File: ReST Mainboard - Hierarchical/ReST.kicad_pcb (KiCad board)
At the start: 2 copper layers, 100 x 100 mm, 190 parts, among them IC1 AT24C256, P1 CONN_01X02, P10 CONN_02X04, P11 CONN_01X04, P12 CONN_01X04, P13 CONN_01X04, P14 CONN_01X04, P15 USB_OTG, P16 CONN_02X05, P17 CONN_02X05, P18 CONN_02X05, P19 CONN_01X04, P2 CONN_01X03, P20 CONN_01X02, P21 CONN_01X04, P22 CONN_02X03, P23 CONN_02X03, P24 CONN_01X04, P25 CONN_02X03, P26 CONN_02X03, P27 CONN_02X06, P28 CONN_02X02, P29 CONN_01X02, P3 CONN_01X02, P30 CONN_01X02, P31 CONN_01X02, P32 CONN_02X02, P33 CONN_02X02, P34 CONN_02X02, P35 CONN_02X03, P36 CONN_02X03, P37 CONN_02X03, P38 CONN_02X03, P39 CONN_02X03, P4 CONN_01X03, P40 CONN_02X04, P5 CONN_01X03, P6 CONN_01X03, P7 CONN_01X03, P8 CONN_01X03, P9 CONN_01X03, Q1 TBD, Q10 Q_AOT240L, Q11 Q_AOT240L, Q12 Q_AOT240L, Q2 TBD, Q3 TBD, Q4 TBD, Q7 Q_BSH105/IRLML2502, Q8 Q_BSH105/IRLML2502, Q9 Q_BSH105/IRLML2502, U10 USBLC6-2, U2 POLOLU_A4988, U3 ACT4088, U4 SC4626, U5 POLOLU_A4988, U6 POLOLU_A4988, U7 POLOLU_A4988, U8 POLOLU_A4988, U9 STM32F10x/STM32F4x, X1 Crystal_Small

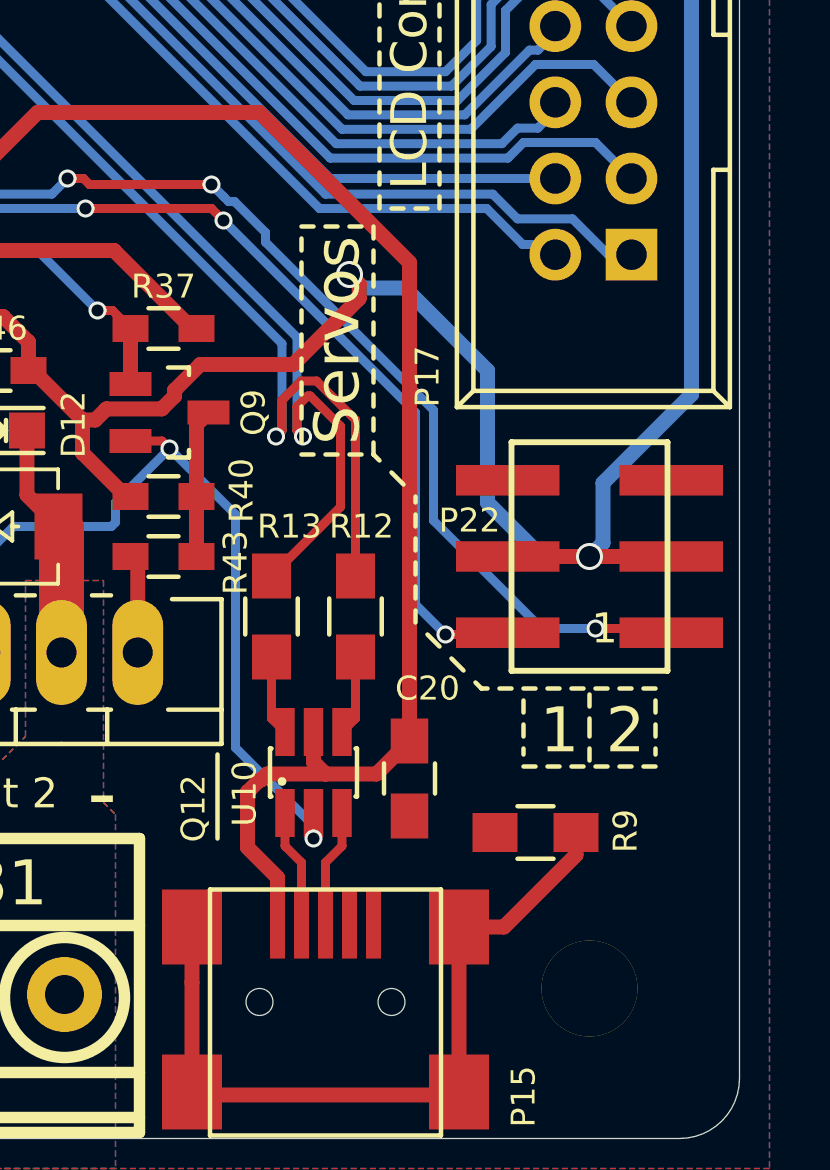
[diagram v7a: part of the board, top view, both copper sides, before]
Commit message: added missing usb pullup
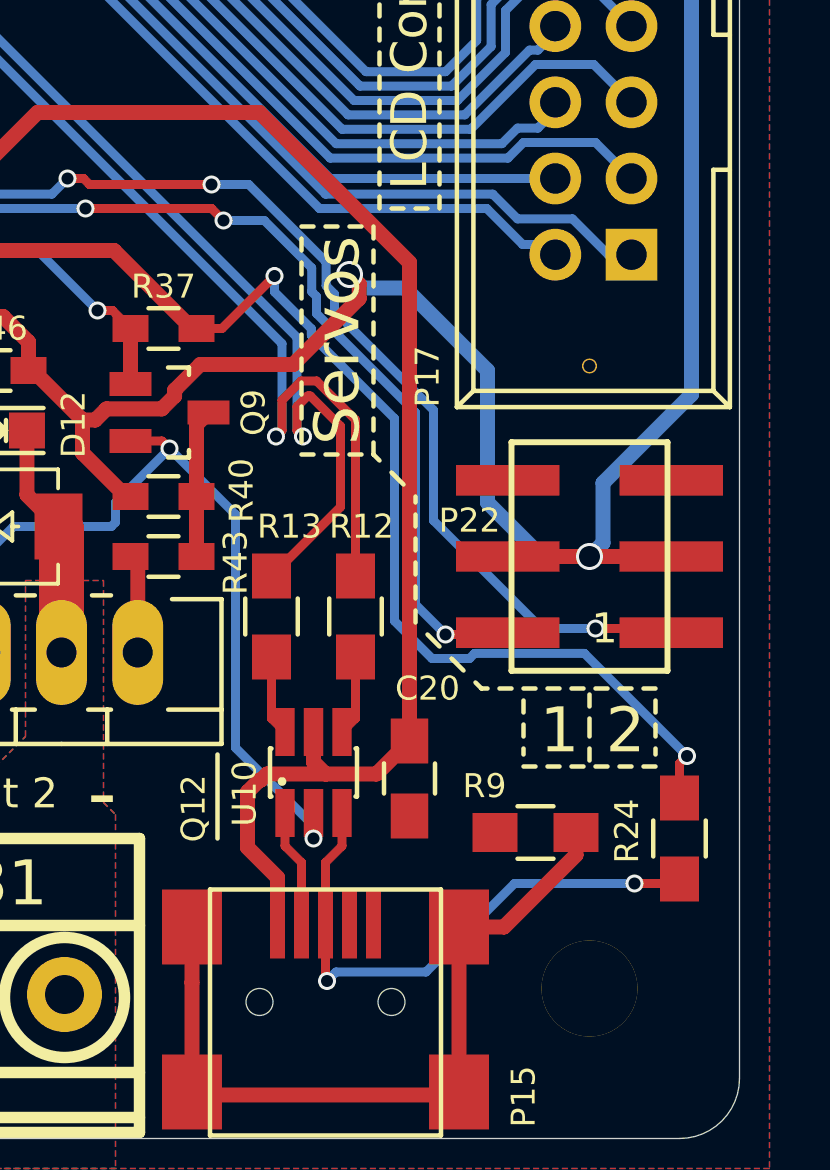
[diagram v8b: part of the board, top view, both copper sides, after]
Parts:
- added R24: 1K5, Resistors_SMD:R_0805_HandSoldering, F.Cu at (117.5, 155.4)
- added REF**: 1pin, ReST-Library:1pin, F.Cu at (114.5, 139.7)
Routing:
- net +3V3: track 502.0 -> 531.8 mm, vias 10 -> 12
- net /Logic/USBP_D+: track 4.03 -> 19.1 mm, vias 0 -> 2
- net SERVO_0: track 58.8 -> 59.6 mm
- net SERVO_1: track 63.0 -> 63.7 mm
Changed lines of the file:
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@@
 (kicad_pcb (version 4) (host pcbnew 4.0.2-stable)
   (general
-    (links 490)
+    (links 492)
     (no_connects 0)
-    (area 18.45 61.641666 122.348 168.25)
+    (area 19.444999 65.444999 119.455001 165.455001)
     (thickness 1.6)
     (drawings 1416)
-    (tracks 2050)
+    (tracks 2083)
     (zones 0)
-    (modules 190)
+    (modules 192)
     (nets 166)
   )
@@
   )
   (module ReST-Library:1pin (layer F.Cu)
+    (at 114.45 139.7)
+    (descr "module 1 pin (ou trou mecanique de percage)")
+    (tags DEV)
+    (zone_connect 2)
+    (fp_text reference REF** (at 0 -0.9) (layer F.SilkS) hide
+      (effects (font (size 1 1) (thickness 0.15)))
+    )
+    (fp_text value 1pin (at 0 1.2) (layer F.Fab)
+      (effects (font (size 1 1) (thickness 0.15)))
+    )
+    (pad GND thru_hole circle (at 0 0) (size 0.5 0.5) (drill 0.4) (layers *.Cu *.Mask F.SilkS)
+      (net 2 GND) (zone_connect 2))
+  )
+  (module ReST-Library:1pin (layer F.Cu)
     (at 86.72 125.7)
     (descr "module 1 pin (ou trou mecanique de percage)")
@@
     (tags "resistor 0805")
     (attr smd)
-    (fp_text reference R9 (at 3 -0.05 90) (layer F.SilkS)
+    (fp_text reference R9 (at -1.7 -1.55 180) (layer F.SilkS)
       (effects (font (size 0.8 0.8) (thickness 0.15)))
     )
@@
       (net 2 GND) (zone_connect 2))
   )
+  (module Resistors_SMD:R_0805_HandSoldering (layer F.Cu)
+    (at 117.45 155.45 90)
+    (descr "Resistor SMD 0805, hand soldering")
+    (tags "resistor 0805")
+    (attr smd)
+    (fp_text reference R24 (at 0.25 -1.75 90) (layer F.SilkS)
+      (effects (font (size 0.8 0.8) (thickness 0.15)))
+    )
+    (fp_text value 1K5 (at 0 2.1 90) (layer F.Fab)
+      (effects (font (size 1 1) (thickness 0.15)))
+    )
+    (fp_line (start -2.4 -1) (end 2.4 -1) (layer F.CrtYd) (width 0.05))
+    (fp_line (start -2.4 1) (end 2.4 1) (layer F.CrtYd) (width 0.05))
+    (fp_line (start -2.4 -1) (end -2.4 1) (layer F.CrtYd) (width 0.05))
+    (fp_line (start 2.4 -1) (end 2.4 1) (layer F.CrtYd) (width 0.05))
+    (fp_line (start 0.6 0.875) (end -0.6 0.875) (layer F.SilkS) (width 0.15))
+    (fp_line (start -0.6 -0.875) (end 0.6 -0.875) (layer F.SilkS) (width 0.15))
+    (pad 1 smd rect (at -1.35 0 90) (size 1.5 1.3) (layers F.Cu F.Paste F.Mask)
+      (net 157 /Logic/USBP_D+))
+    (pad 2 smd rect (at 1.35 0 90) (size 1.5 1.3) (layers F.Cu F.Paste F.Mask)
+      (net 3 +3V3))
+    (model Resistors_SMD.3dshapes/R_0805_HandSoldering.wrl
+      (at (xyz 0 0 0))
+      (scale (xyz 1 1 1))
+      (rotate (xyz 0 0 0))
+    )
+  )
   (gr_line (start 119.45 163.45) (end 119.45 67.45) (layer Edge.Cuts) (width 0.01))
   (gr_line (start 21.45 165.45) (end 117.45 165.45) (layer Edge.Cuts) (width 0.01))
@@
   (segment (start 84.5491 115.7241) (end 85.875 117.05) (width 0.3) (layer F.Cu) (net 2))
   (segment (start 85.875 117.05) (end 86 117.05) (width 0.3) (layer F.Cu) (net 2))
+  (segment (start 103.95 136.7) (end 102.2 138.45) (width 0.3) (layer F.Cu) (net 3))
+  (segment (start 102.2 138.45) (end 101.35 138.45) (width 0.3) (layer F.Cu) (net 3))
+  (segment (start 105.180009 138.680009) (end 105.180009 138.458845) (width 0.3) (layer B.Cu) (net 3))
+  (segment (start 105.180009 138.458845) (end 103.95 137.228836) (width 0.3) (layer B.Cu) (net 3))
+  (segment (start 103.95 137.228836) (end 103.95 136.7) (width 0.3) (layer B.Cu) (net 3))
+  (via (at 103.95 136.7) (size 0.6) (drill 0.4) (layers F.Cu B.Cu) (net 3))
+  (segment (start 107.95 142.95) (end 107.95 141.45) (width 0.3) (layer B.Cu) (net 3))
+  (segment (start 107.95 141.45) (end 105.180009 138.680009) (width 0.3) (layer B.Cu) (net 3))
+  (segment (start 105.180009 138.680009) (end 105.180009 138.547621) (width 0.3) (layer B.Cu) (net 3))
+  (segment (start 107.95 148.2) (end 107.95 142.95) (width 0.3) (layer B.Cu) (net 3))
+  (segment (start 109.2 149.45) (end 107.95 148.2) (width 0.3) (layer B.Cu) (net 3))
+  (segment (start 110.45 149.45) (end 109.2 149.45) (width 0.3) (layer B.Cu) (net 3))
+  (segment (start 110.619999 149.280001) (end 110.45 149.45) (width 0.3) (layer B.Cu) (net 3))
+  (segment (start 117.7 152.7) (end 114.280001 149.280001) (width 0.3) (layer B.Cu) (net 3))
+  (segment (start 114.280001 149.280001) (end 110.619999 149.280001) (width 0.3) (layer B.Cu) (net 3))
+  (segment (start 117.45 154.1) (end 117.45 152.95) (width 0.3) (layer F.Cu) (net 3))
+  (via (at 117.7 152.7) (size 0.6) (drill 0.4) (layers F.Cu B.Cu) (net 3))
+  (segment (start 117.45 152.95) (end 117.7 152.7) (width 0.3) (layer F.Cu) (net 3))
   (segment (start 101.65 110.175) (end 100.975 110.175) (width 0.3) (layer F.Cu) (net 3))
   (segment (start 101.65 110.175) (end 101.675 110.15) (width 0.3) (layer F.Cu) (net 3))
@@
   (segment (start 93.051174 100.36999) (end 89.570524 103.85064) (width 0.3) (layer F.Cu) (net 59))
   (segment (start 89.570524 103.85064) (end 87 103.85064) (width 0.3) (layer F.Cu) (net 59))
+  (segment (start 105.669999 136.230001) (end 103.089998 133.65) (width 0.3) (layer B.Cu) (net 60))
+  (segment (start 103.089998 133.65) (end 101.85 133.65) (width 0.3) (layer B.Cu) (net 60))
+  (segment (start 105.95 137.871164) (end 109.25 141.171164) (width 0.3) (layer B.Cu) (net 60))
+  (segment (start 105.95 137.871164) (end 105.95 137.304402) (width 0.3) (layer B.Cu) (net 60))
+  (segment (start 105.95 137.304402) (end 105.669999 137.024401) (width 0.3) (layer B.Cu) (net 60))
+  (segment (start 105.669999 137.024401) (end 105.669999 136.230001) (width 0.3) (layer B.Cu) (net 60))
   (segment (start 114.65 148.45) (end 117.035 148.45) (width 0.3) (layer F.Cu) (net 60))
   (segment (start 117.035 148.45) (end 117.175 148.59) (width 0.3) (layer F.Cu) (net 60))
@@
   (via (at 114.65 148.45) (size 0.6) (drill 0.4) (layers F.Cu B.Cu) (net 60))
   (segment (start 109.25 141.171164) (end 109.25 144.85) (width 0.3) (layer B.Cu) (net 60))
-  (segment (start 103.65 135.571164) (end 109.25 141.171164) (width 0.3) (layer B.Cu) (net 60))
-  (segment (start 102.619999 134.219999) (end 103.65 135.25) (width 0.3) (layer B.Cu) (net 60))
-  (segment (start 103.65 135.25) (end 103.65 135.571164) (width 0.3) (layer B.Cu) (net 60))
-  (segment (start 102.25 134.05) (end 102.419999 134.219999) (width 0.3) (layer B.Cu) (net 60))
-  (segment (start 102.419999 134.219999) (end 102.619999 134.219999) (width 0.3) (layer B.Cu) (net 60))
-  (segment (start 101.85 133.65) (end 102.25 134.05) (width 0.3) (layer B.Cu) (net 60))
   (segment (start 97.05 133.45) (end 97.582402 133.45) (width 0.3) (layer F.Cu) (net 60))
   (segment (start 97.582402 133.45) (end 97.782402 133.65) (width 0.3) (layer F.Cu) (net 60))
@@
   (via (at 81.45 111.85) (size 0.6) (drill 0.4) (layers F.Cu B.Cu) (net 60))
   (segment (start 81.04898 112.25102) (end 81.45 111.85) (width 0.3) (layer F.Cu) (net 60))
-  (segment (start 109.65 148.65) (end 111.665 148.65) (width 0.3) (layer F.Cu) (net 61))
-  (segment (start 111.665 148.65) (end 111.725 148.59) (width 0.3) (layer F.Cu) (net 61))
+  (segment (start 102.25 134.85) (end 103.611162 134.85) (width 0.3) (layer B.Cu) (net 61))
+  (segment (start 103.611162 134.85) (end 105.189989 136.428827) (width 0.3) (layer B.Cu) (net 61))
+  (segment (start 105.189989 136.428827) (end 105.189989 137.223227) (width 0.3) (layer B.Cu) (net 61))
   (segment (start 108.65 141.25) (end 108.65 147.65) (width 0.3) (layer B.Cu) (net 61))
+  (segment (start 105.189989 137.223227) (end 105.35 137.383238) (width 0.3) (layer B.Cu) (net 61))
+  (segment (start 105.35 137.383238) (end 105.35 137.95) (width 0.3) (layer B.Cu) (net 61))
+  (segment (start 105.35 137.95) (end 108.65 141.25) (width 0.3) (layer B.Cu) (net 61))
   (segment (start 108.65 147.65) (end 109.65 148.65) (width 0.3) (layer B.Cu) (net 61))
+  (segment (start 109.65 148.65) (end 111.665 148.65) (width 0.3) (layer F.Cu) (net 61))
+  (segment (start 111.665 148.65) (end 111.725 148.59) (width 0.3) (layer F.Cu) (net 61))
   (via (at 109.65 148.65) (size 0.6) (drill 0.4) (layers F.Cu B.Cu) (net 61))
-  (segment (start 102.25 134.85) (end 108.65 141.25) (width 0.3) (layer B.Cu) (net 61))
   (segment (start 97.65 134.45) (end 101.85 134.45) (width 0.3) (layer F.Cu) (net 61))
   (segment (start 101.85 134.45) (end 102.25 134.85) (width 0.3) (layer F.Cu) (net 61))
@@
   (segment (start 104.8499 156.2499) (end 104.8499 156.95006) (width 0.3) (layer F.Cu) (net 156))
   (segment (start 104.8499 156.95006) (end 104.8499 158.40068) (width 0.3) (layer F.Cu) (net 156))
+  (segment (start 115.95 156.95) (end 117.3 156.95) (width 0.3) (layer F.Cu) (net 157))
+  (segment (start 117.3 156.95) (end 117.45 156.8) (width 0.3) (layer F.Cu) (net 157))
+  (segment (start 111.95 156.95) (end 115.95 156.95) (width 0.3) (layer B.Cu) (net 157))
+  (via (at 115.95 156.95) (size 0.6) (drill 0.4) (layers F.Cu B.Cu) (net 157))
+  (segment (start 108.999999 159.900001) (end 111.95 156.95) (width 0.3) (layer B.Cu) (net 157))
+  (segment (start 105.7 160.2) (end 105.999999 159.900001) (width 0.3) (layer B.Cu) (net 157))
+  (segment (start 105.999999 159.900001) (end 108.999999 159.900001) (width 0.3) (layer B.Cu) (net 157))
+  (segment (start 105.65 158.30068) (end 105.65 160.15) (width 0.3) (layer F.Cu) (net 157))
+  (segment (start 105.65 160.15) (end 105.7 160.2) (width 0.3) (layer F.Cu) (net 157))
+  (via (at 105.7 160.2) (size 0.6) (drill 0.4) (layers F.Cu B.Cu) (net 157))
   (segment (start 106.2 154.6) (end 106.2 155.7) (width 0.3) (layer F.Cu) (net 157))
   (segment (start 106.2 155.7) (end 105.65 156.25) (width 0.3) (layer F.Cu) (net 157))
